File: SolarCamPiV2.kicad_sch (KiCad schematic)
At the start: 78 parts, among them Q2 AO3401A, Q3 2N7002, Q4 AO3401A, Q5 2N7002, Q6 BSS84, U1 CN3767, U2 HT7533, U3 SY8113B

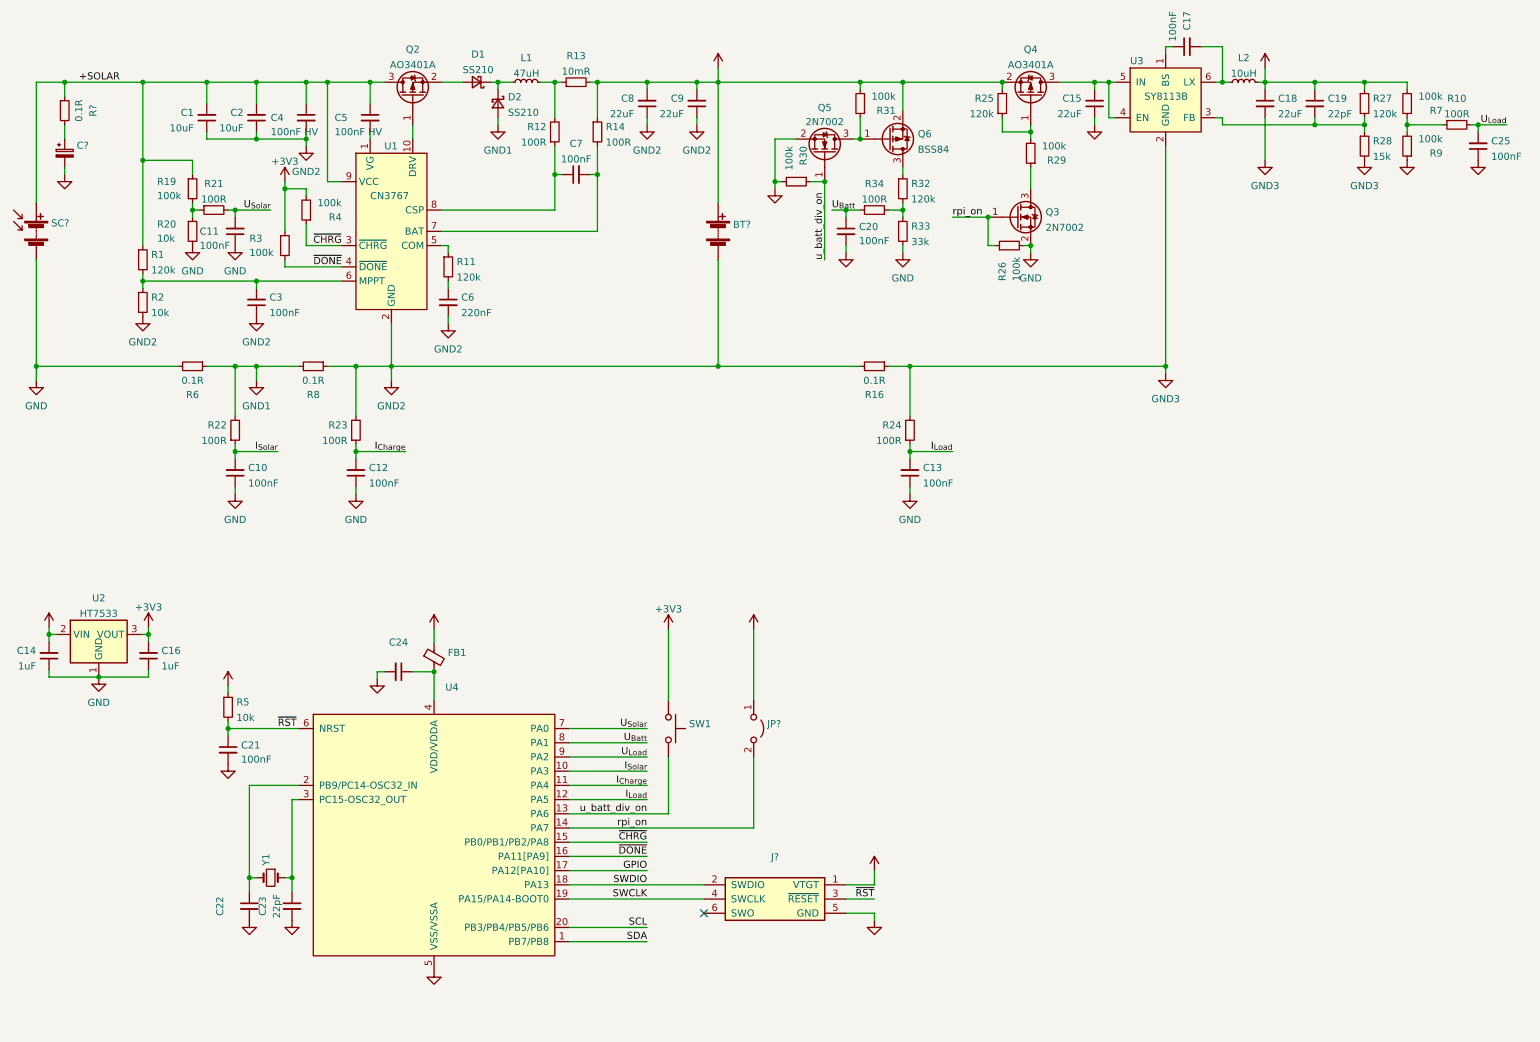
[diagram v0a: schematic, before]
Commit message: Add RPi socket
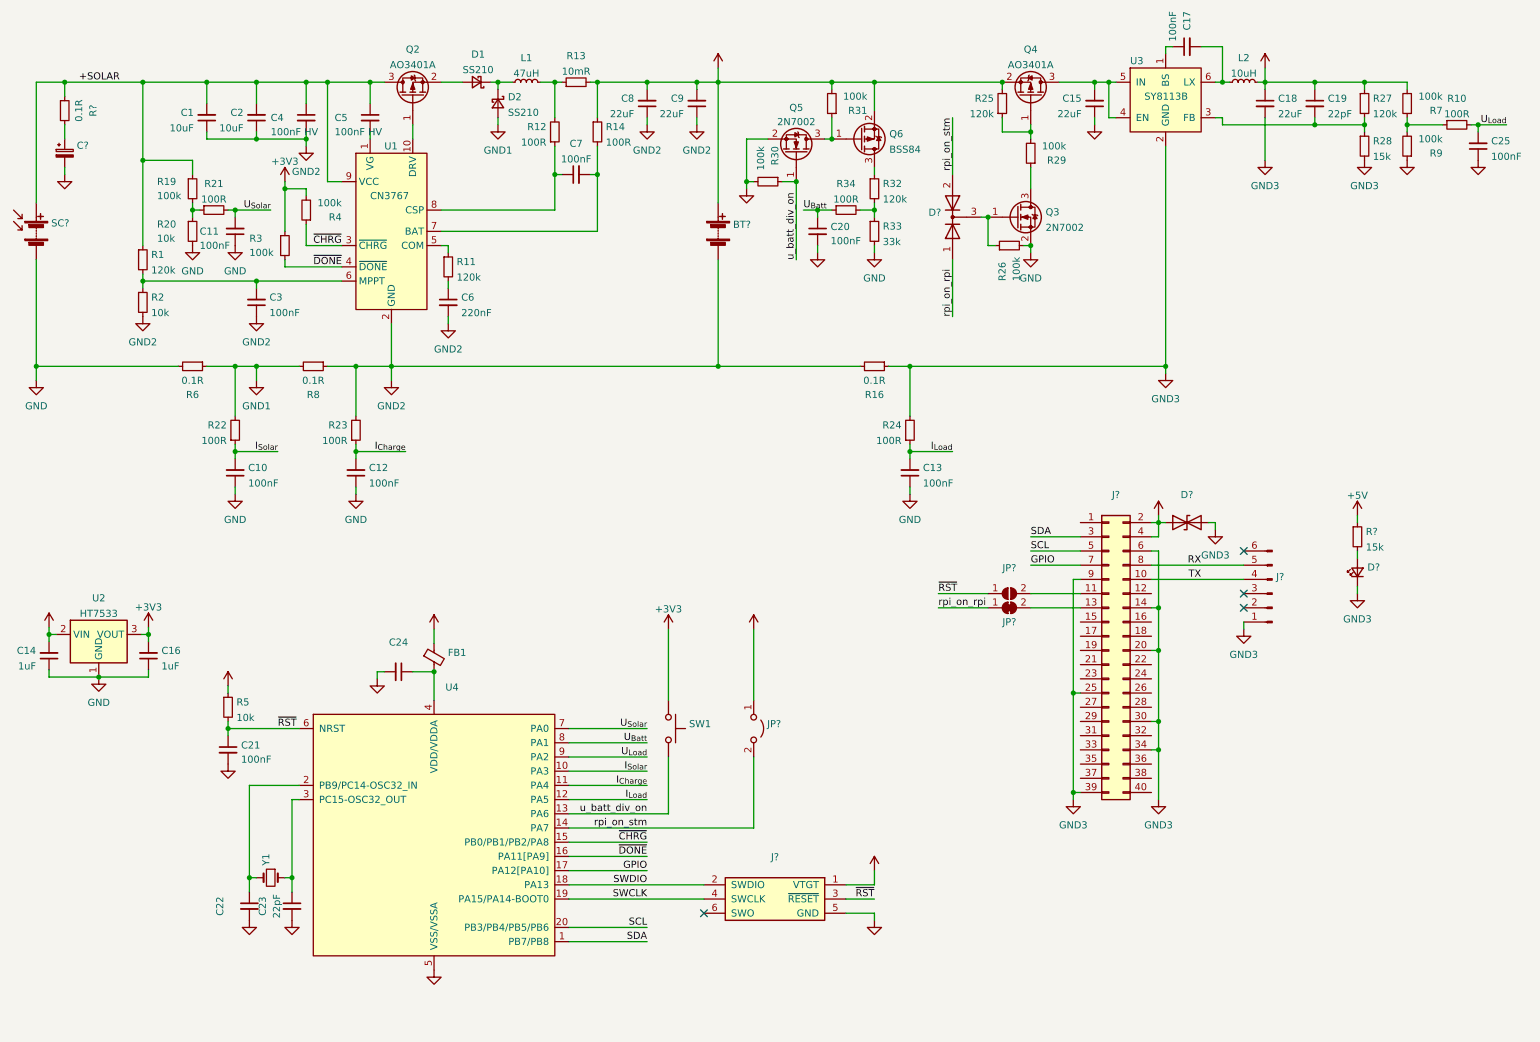
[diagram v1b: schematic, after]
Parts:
- added D?: (no value), symbol Device:D_TVS
- added D?: (no value), symbol Diode:BAV70
- added D?: (no value), symbol Device:LED_Small
- added J?: (no value), symbol Connector_Generic:Conn_02x20_Odd_Even
- added J?: (no value), symbol Connector:Conn_01x06_Male
- added JP?: (no value), symbol Jumper:SolderJumper_2_Bridged
- added JP?: (no value), symbol Jumper:SolderJumper_2_Open
- added R?: 15k, Resistor_SMD:R_0402_1005Metric, symbol Device:R_Small
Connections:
- net +5V: now also D?.1 (A1), J?.2 (Pin_2), J?.4 (Pin_4), R?.1
- net GND3: now also D?.1 (K), D?.2 (A2), J?.1 (Pin_1), J?.14 (Pin_14), J?.20 (Pin_20), J?.25 (Pin_25), J?.30 (Pin_30), J?.34 (Pin_34), J?.39 (Pin_39), J?.6 (Pin_6), J?.9 (Pin_9)
- net GPIO: now also J?.7 (Pin_7)
- net SCL: now also J?.5 (Pin_5)
- net SDA: now also J?.3 (Pin_3)
- net ~{RST}: now also JP?.1 (A)
- net rpi_on: no longer names the net of Q3.1 (G), R26.1
- net rpi_on: now also D?.3 (K); no longer JP?.2 (B), U4.14 (PA7)
- new net: D?.2 (A), R?.2
- new net: J?.13 (Pin_13), JP?.2 (B)
- new net: J?.11 (Pin_11), JP?.2 (B)
- new net RX: J?.5 (Pin_5), J?.8 (Pin_8)
- new net TX: J?.10 (Pin_10), J?.4 (Pin_4)
- new net rpi_on_rpi: D?.1 (A), JP?.1 (A)
- new net rpi_on_stm: D?.2 (A), JP?.2 (B), U4.14 (PA7)
- no-connect marks 1 -> 4
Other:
- moved on the sheet: C20, Q5, Q6, R30, R31, R32, R33, R34

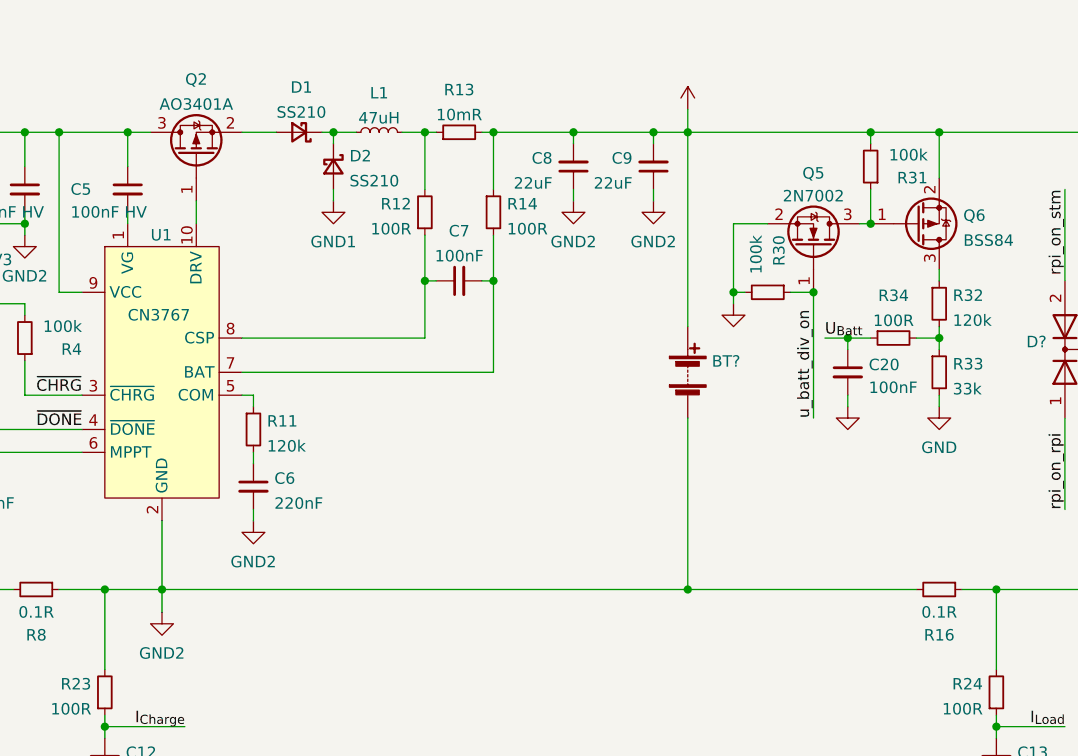
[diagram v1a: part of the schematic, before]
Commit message: Change MTTP charge current setpoint to 1.2A
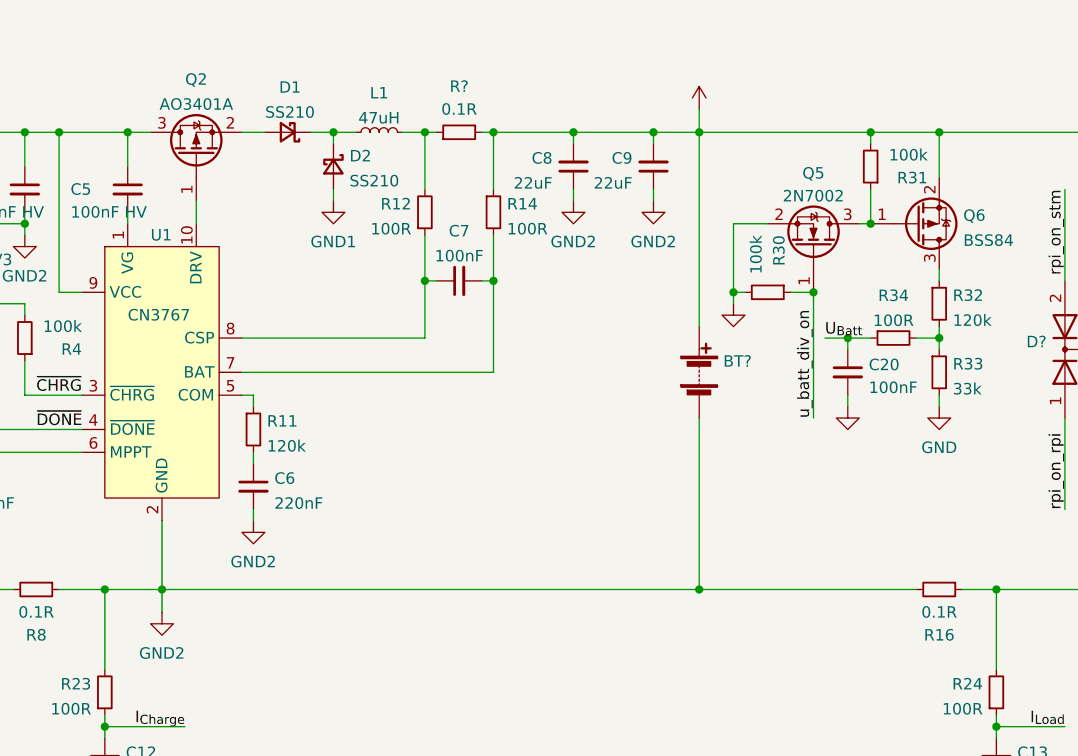
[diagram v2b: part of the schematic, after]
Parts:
- removed R13: 10mR, Resistor_SMD:R_2512_6332Metric, symbol Device:R_Small
- added R?: 0.1R, Resistor_SMD:R_1206_3216Metric, symbol Device:R_Small
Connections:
- net +BATT: now also R?.2
- net at L1.2, R12.2: now also R?.1
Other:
- moved on the sheet: BT?, D1
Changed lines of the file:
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@@
 (kicad_sch (version 20211123) (generator eeschema)
   (paper "A4")
+  (junction (at 140.97 27.94) (diameter 0) (color 0 0 0 0)
+  )
   (junction (at 22.86 27.94) (diameter 0) (color 0 0 0 0)
   )
@@
   (junction (at 167.64 27.94) (diameter 0) (color 0 0 0 0)
   )
-  (junction (at 139.7 78.74) (diameter 0) (color 0 0 0 0)
-  )
   (junction (at 53.34 93.98) (diameter 0) (color 0 0 0 0)
   )
@@
   (junction (at 110.49 44.45) (diameter 0) (color 0 0 0 0)
   )
-  (junction (at 139.7 27.94) (diameter 0) (color 0 0 0 0)
-  )
   (junction (at 160.02 27.94) (diameter 0) (color 0 0 0 0)
   )
@@
   (junction (at 218.44 129.54) (diameter 0) (color 0 0 0 0)
   )
+  (junction (at 140.97 78.74) (diameter 0) (color 0 0 0 0)
+  )
   (junction (at 77.47 27.94) (diameter 0) (color 0 0 0 0)
   )
@@
     (stroke (width 0) (type default) (color 0 0 0 0))
   )
-  (wire (pts (xy 90.17 27.94) (xy 93.98 27.94))
-    (stroke (width 0) (type default) (color 0 0 0 0))
-  )
   (wire (pts (xy 85.09 35.56) (xy 85.09 38.1))
     (stroke (width 0) (type default) (color 0 0 0 0))
@@
     (stroke (width 0) (type default) (color 0 0 0 0))
   )
-  (wire (pts (xy 139.7 59.69) (xy 139.7 78.74))
+  (wire (pts (xy 140.97 59.69) (xy 140.97 78.74))
     (stroke (width 0) (type default) (color 0 0 0 0))
   )
@@
     (stroke (width 0) (type default) (color 0 0 0 0))
   )
-  (wire (pts (xy 139.7 78.74) (xy 165.1 78.74))
-    (stroke (width 0) (type default) (color 0 0 0 0))
-  )
   (wire (pts (xy 53.34 100.33) (xy 53.34 101.6))
     (stroke (width 0) (type default) (color 0 0 0 0))
@@
     (stroke (width 0) (type default) (color 0 0 0 0))
   )
-  (wire (pts (xy 139.7 27.94) (xy 135.89 27.94))
-    (stroke (width 0) (type default) (color 0 0 0 0))
-  )
   (wire (pts (xy 157.48 50.8) (xy 157.48 52.07))
     (stroke (width 0) (type default) (color 0 0 0 0))
@@
     (stroke (width 0) (type default) (color 0 0 0 0))
   )
+  (wire (pts (xy 90.17 27.94) (xy 92.71 27.94))
+    (stroke (width 0) (type default) (color 0 0 0 0))
+  )
   (wire (pts (xy 66.04 36.83) (xy 66.04 38.1))
     (stroke (width 0) (type default) (color 0 0 0 0))
@@
     (stroke (width 0) (type default) (color 0 0 0 0))
   )
-  (wire (pts (xy 81.28 78.74) (xy 139.7 78.74))
+  (wire (pts (xy 81.28 78.74) (xy 140.97 78.74))
     (stroke (width 0) (type default) (color 0 0 0 0))
   )
@@
     (stroke (width 0) (type default) (color 0 0 0 0))
   )
-  (wire (pts (xy 139.7 25.4) (xy 139.7 27.94))
+  (wire (pts (xy 140.97 25.4) (xy 140.97 27.94))
     (stroke (width 0) (type default) (color 0 0 0 0))
   )
@@
     (stroke (width 0) (type default) (color 0 0 0 0))
   )
+  (wire (pts (xy 140.97 78.74) (xy 165.1 78.74))
+    (stroke (width 0) (type default) (color 0 0 0 0))
+  )
   (wire (pts (xy 217.17 116.84) (xy 233.68 116.84))
     (stroke (width 0) (type default) (color 0 0 0 0))
@@
     (stroke (width 0) (type default) (color 0 0 0 0))
   )
-  (wire (pts (xy 139.7 27.94) (xy 139.7 49.53))
+  (wire (pts (xy 140.97 27.94) (xy 140.97 49.53))
     (stroke (width 0) (type default) (color 0 0 0 0))
   )
@@
     (stroke (width 0) (type default) (color 0 0 0 0))
   )
-  (wire (pts (xy 99.06 27.94) (xy 100.33 27.94))
+  (wire (pts (xy 97.79 27.94) (xy 100.33 27.94))
     (stroke (width 0) (type default) (color 0 0 0 0))
   )
@@
     (stroke (width 0) (type default) (color 0 0 0 0))
   )
-  (wire (pts (xy 139.7 27.94) (xy 160.02 27.94))
+  (wire (pts (xy 135.89 27.94) (xy 140.97 27.94))
     (stroke (width 0) (type default) (color 0 0 0 0))
   )
@@
     (stroke (width 0) (type default) (color 0 0 0 0))
   )
+  (wire (pts (xy 140.97 27.94) (xy 160.02 27.94))
+    (stroke (width 0) (type default) (color 0 0 0 0))
+  )
   (wire (pts (xy 246.38 27.94) (xy 255.27 27.94))
     (stroke (width 0) (type default) (color 0 0 0 0))
@@
     (pin "2")
   )
-  (symbol (lib_id "power:+BATT") (at 139.7 25.4 0) (unit 1)
-    (in_bom yes) (on_board yes) (fields_autoplaced)
-    (property "Reference" "#PWR?" (id 0) (at 139.7 29.21 0)
+  (symbol (lib_id "power:+BATT") (at 140.97 25.4 0) (unit 1)
+    (in_bom yes) (on_board yes)
+    (property "Reference" "#PWR?" (id 0) (at 140.97 29.21 0)
       (effects (font (size 1.27 1.27)) hide)
     )
-    (property "Value" "" (id 1) (at 139.7 21.8242 0))
-    (property "Footprint" "" (id 2) (at 139.7 25.4 0)
+    (property "Value" "" (id 1) (at 142.24 21.8242 0))
+    (property "Footprint" "" (id 2) (at 140.97 25.4 0)
       (effects (font (size 1.27 1.27)) hide)
     )
-    (property "Datasheet" "" (id 3) (at 139.7 25.4 0)
+    (property "Datasheet" "" (id 3) (at 140.97 25.4 0)
       (effects (font (size 1.27 1.27)) hide)
     )
@@
     (pin "2")
   )
+  (symbol (lib_id "Device:R_Small") (at 114.3 27.94 90) (unit 1)
+    (in_bom yes) (on_board yes)
+    (property "Reference" "R?" (id 0) (at 114.3 22.86 90))
+    (property "Value" "0.1R" (id 1) (at 114.3 25.4 90))
+    (property "Footprint" "Resistor_SMD:R_1206_3216Metric" (id 2) (at 114.3 27.94 0)
+      (effects (font (size 1.27 1.27)) hide)
+    )
+    (property "Datasheet" "~" (id 3) (at 114.3 27.94 0)
+      (effects (font (size 1.27 1.27)) hide)
+    )
+    (property "LCSC" "C25334" (id 4) (at 114.3 27.94 90)
+      (effects (font (size 1.27 1.27)) hide)
+    )
+    (pin "1")
+    (pin "2")
+  )
   (symbol (lib_id "Device:FerriteBead_Small") (at 88.9 130.81 0) (unit 1)
     (in_bom yes) (on_board yes) (fields_autoplaced)
@@
     (pin "2")
   )
-  (symbol (lib_id "Device:D_Schottky_Small") (at 96.52 27.94 180) (unit 1)
+  (symbol (lib_id "Device:D_Schottky_Small") (at 95.25 27.94 180) (unit 1)
     (in_bom yes) (on_board yes) (fields_autoplaced)
-    (property "Reference" "D1" (id 0) (at 96.774 22.9575 0))
-    (property "Value" "SS210" (id 1) (at 96.774 25.7326 0))
-    (property "Footprint" "Diode_SMD:D_SMA" (id 2) (at 96.52 27.94 90)
+    (property "Reference" "D1" (id 0) (at 95.504 22.9575 0))
+    (property "Value" "SS210" (id 1) (at 95.504 25.7326 0))
+    (property "Footprint" "Diode_SMD:D_SMA" (id 2) (at 95.25 27.94 90)
       (effects (font (size 1.27 1.27)) hide)
     )
-    (property "Datasheet" "~" (id 3) (at 96.52 27.94 90)
+    (property "Datasheet" "~" (id 3) (at 95.25 27.94 90)
       (effects (font (size 1.27 1.27)) hide)
     )
-    (property "LCSC" "C14996" (id 4) (at 96.52 27.94 0)
+    (property "LCSC" "C14996" (id 4) (at 95.25 27.94 0)
       (effects (font (size 1.27 1.27)) hide)
     )
@@
     (pin "1")
   )
-  (symbol (lib_id "Device:R_Small") (at 114.3 27.94 90) (unit 1)
-    (in_bom yes) (on_board yes) (fields_autoplaced)
-    (property "Reference" "R13" (id 0) (at 114.3 23.2369 90))
-    (property "Value" "10mR" (id 1) (at 114.3 26.012 90))
-    (property "Footprint" "Resistor_SMD:R_2512_6332Metric" (id 2) (at 114.3 27.94 0)
-      (effects (font (size 1.27 1.27)) hide)
-    )
-    (property "Datasheet" "~" (id 3) (at 114.3 27.94 0)
-      (effects (font (size 1.27 1.27)) hide)
-    )
-    (property "LCSC" "C127692" (id 4) (at 114.3 27.94 90)
-      (effects (font (size 1.27 1.27)) hide)
-    )
-    (pin "1")
-    (pin "2")
-  )
   (symbol (lib_id "power:GND1") (at 100.33 35.56 0) (unit 1)
     (in_bom yes) (on_board yes) (fields_autoplaced)
@@
     (pin "1")
   )
-  (symbol (lib_id "Device:Battery") (at 139.7 54.61 0) (unit 1)
+  (symbol (lib_id "Device:Battery") (at 140.97 54.61 0) (unit 1)
     (in_bom yes) (on_board yes) (fields_autoplaced)
-    (property "Reference" "BT?" (id 0) (at 142.367 53.3943 0)
+    (property "Reference" "BT?" (id 0) (at 143.637 53.3943 0)
       (effects (font (size 1.27 1.27)) (justify left))
     )
-    (property "Value" "" (id 1) (at 142.367 55.9312 0)
+    (property "Value" "" (id 1) (at 143.637 55.9312 0)
       (effects (font (size 1.27 1.27)) (justify left))
     )
-    (property "Footprint" "" (id 2) (at 139.7 53.086 90)
+    (property "Footprint" "" (id 2) (at 140.97 53.086 90)
       (effects (font (size 1.27 1.27)) hide)
     )
-    (property "Datasheet" "~" (id 3) (at 139.7 53.086 90)
+    (property "Datasheet" "~" (id 3) (at 140.97 53.086 90)
       (effects (font (size 1.27 1.27)) hide)
     )
@@
       (reference "R12") (unit 1) (value "100R") (footprint "Resistor_SMD:R_0402_1005Metric")
     )
-    (path "/ac56b332-b38a-4799-9b06-cbb8f2747fe9"
-      (reference "R13") (unit 1) (value "10mR") (footprint "Resistor_SMD:R_2512_6332Metric")
-    )
     (path "/42ae477d-7f99-4b72-a624-4ae6cc935b51"
       (reference "R14") (unit 1) (value "100R") (footprint "Resistor_SMD:R_0402_1005Metric")
@@
       (reference "R?") (unit 1) (value "15k") (footprint "Resistor_SMD:R_0402_1005Metric")
     )
+    (path "/7d9ce857-ecca-48df-9b84-ce78fcb51947"
+      (reference "R?") (unit 1) (value "0.1R") (footprint "Resistor_SMD:R_1206_3216Metric")
+    )
     (path "/c272654b-2781-4dcd-ab85-f5f4b055127d"
